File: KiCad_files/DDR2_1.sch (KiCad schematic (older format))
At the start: 13 parts, among them J10 AS4C128M16D2A

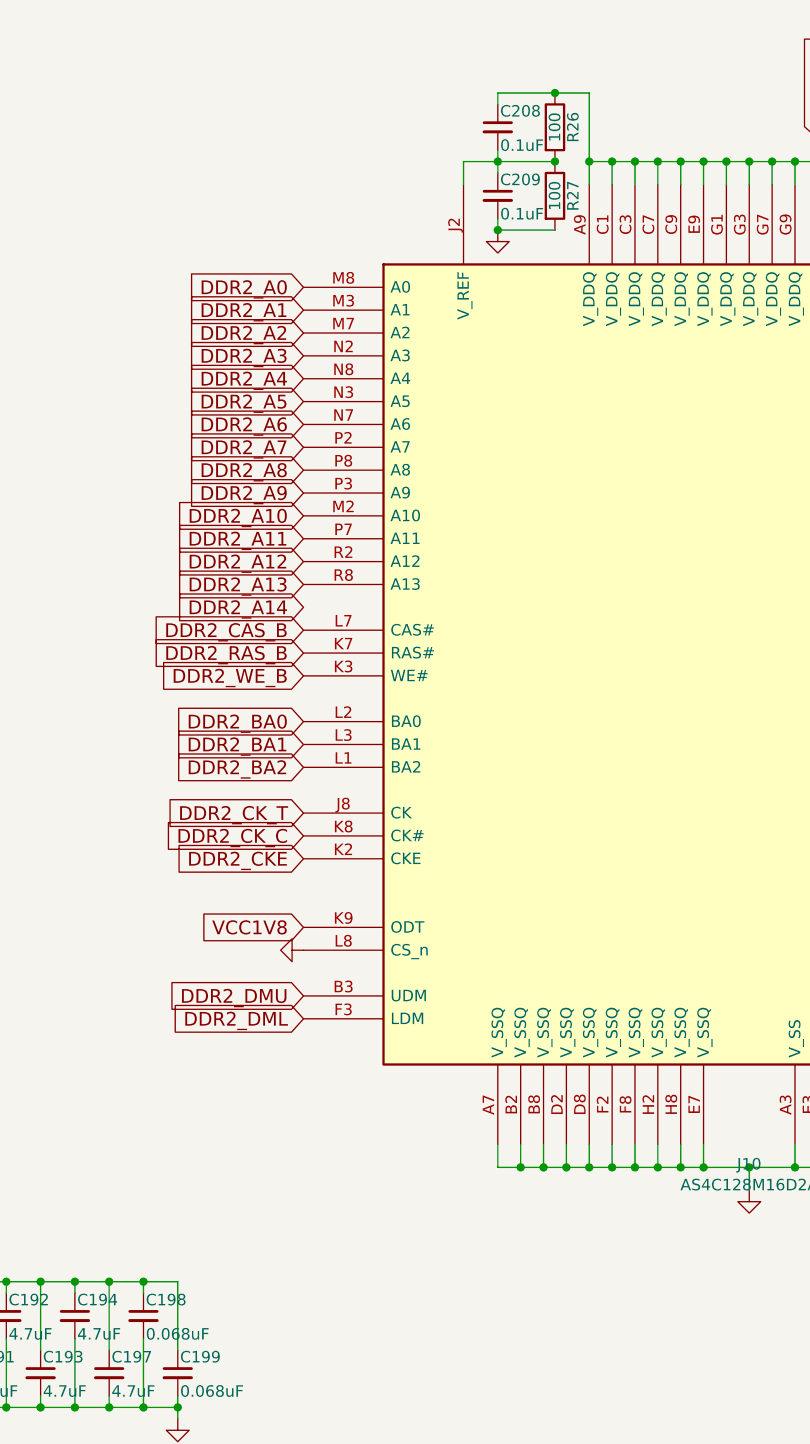
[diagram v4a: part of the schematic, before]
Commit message: More caps and added lots of test points
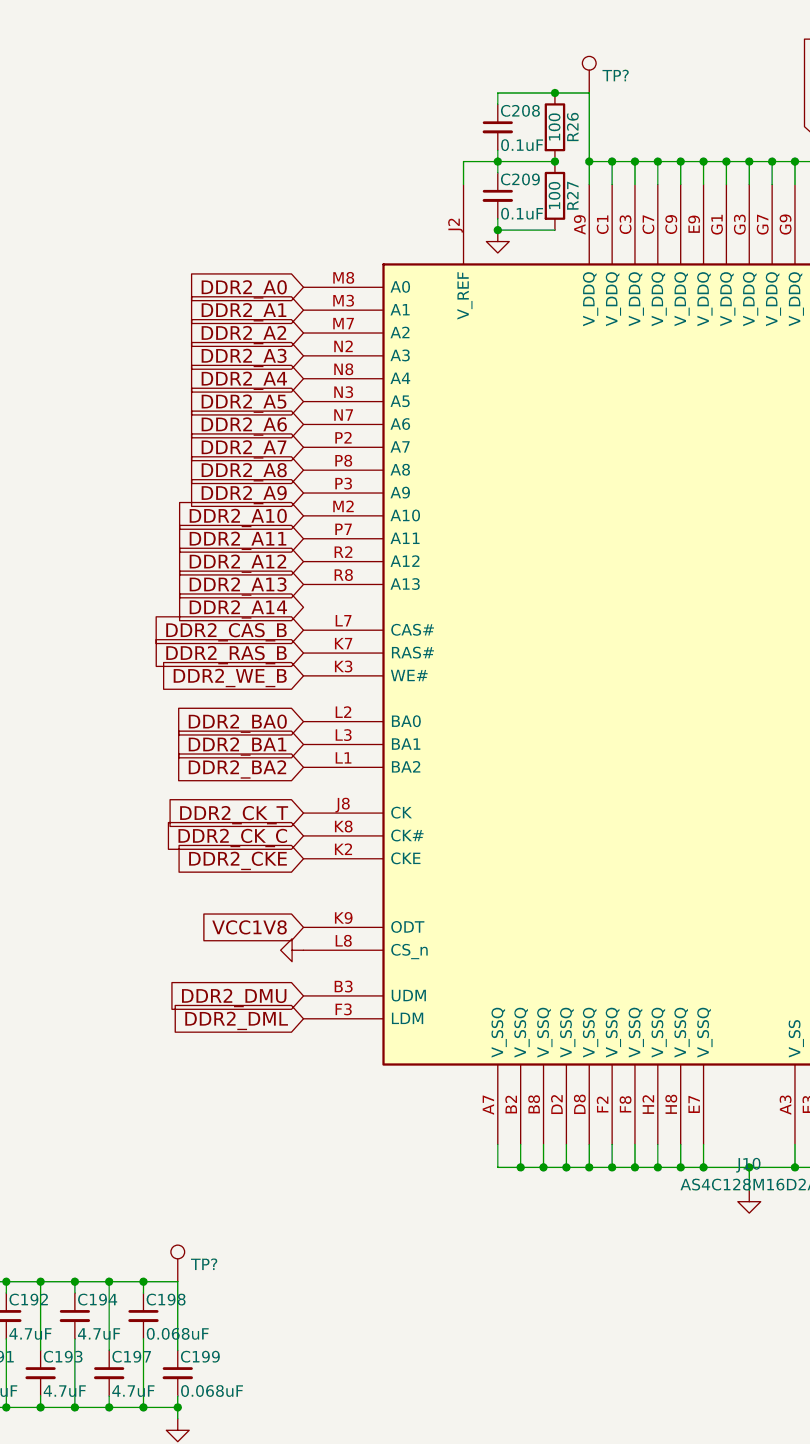
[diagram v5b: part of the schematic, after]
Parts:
- added TP? (x2): TestPoint, symbol Connector:TestPoint
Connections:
- net VCC1V8: now also TP?.1, TP?.1
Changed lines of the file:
@@
+	1    0    0    -1
+$EndComp
+$Comp
+L Connector:TestPoint TP?
+U 1 1 5CE9365C
+P 3400 6550
+F 0 "TP?" H 3458 6624 50  0000 L CNN
+F 1 "TestPoint" H 3458 6579 50  0001 L CNN
+F 2 "" H 3600 6550 50  0001 C CNN
+F 3 "~" H 3600 6550 50  0001 C CNN
+	1    3400 6550
+	1    0    0    -1
+$EndComp
+$Comp
+L Connector:TestPoint TP?
+U 1 1 5CE96F0C
+P 5200 1350
+F 0 "TP?" H 5258 1424 50  0000 L CNN
+F 1 "TestPoint" H 5258 1379 50  0001 L CNN
+F 2 "" H 5400 1350 50  0001 C CNN
+F 3 "~" H 5400 1350 50  0001 C CNN
+	1    5200 1350
 	1    0    0    -1
 $EndComp

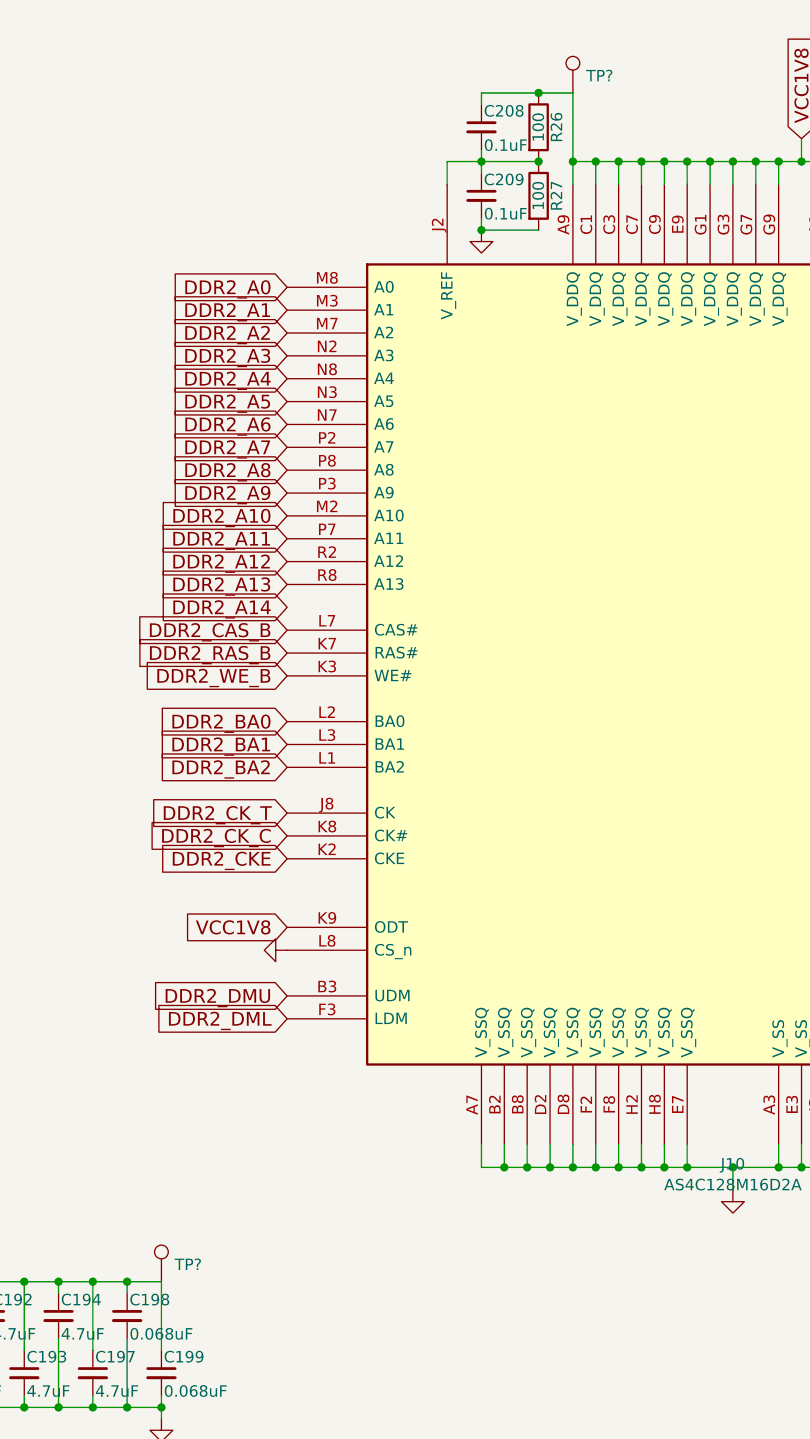
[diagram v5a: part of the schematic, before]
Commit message: Annotations and proper connections
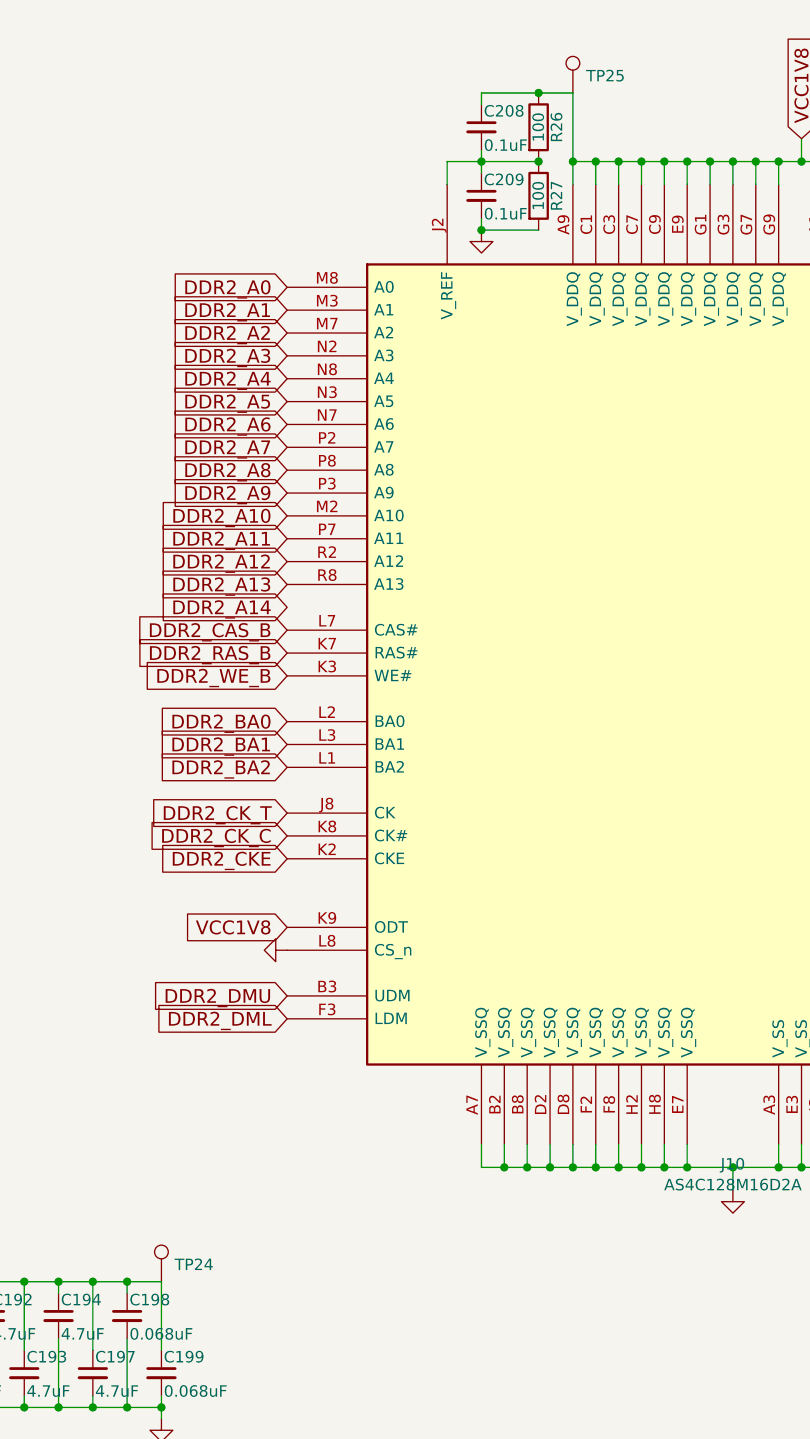
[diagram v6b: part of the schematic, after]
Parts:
- gave numbers to parts that had none: 2
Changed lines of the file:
@@
 U 1 1 5CE9365C
 P 3400 6550
-F 0 "TP?" H 3458 6624 50  0000 L CNN
+AR Path="/5BFDDAF0/5CE9365C" Ref="TP?"  Part="1"
+AR Path="/5C0652F6/5CE9365C" Ref="TP24"  Part="1"
+F 0 "TP24" H 3458 6624 50  0000 L CNN
 F 1 "TestPoint" H 3458 6579 50  0001 L CNN
 F 2 "" H 3600 6550 50  0001 C CNN
@@
 U 1 1 5CE96F0C
 P 5200 1350
-F 0 "TP?" H 5258 1424 50  0000 L CNN
+AR Path="/5BFDDAF0/5CE96F0C" Ref="TP?"  Part="1"
+AR Path="/5C0652F6/5CE96F0C" Ref="TP25"  Part="1"
+F 0 "TP25" H 5258 1424 50  0000 L CNN
 F 1 "TestPoint" H 5258 1379 50  0001 L CNN
 F 2 "" H 5400 1350 50  0001 C CNN
